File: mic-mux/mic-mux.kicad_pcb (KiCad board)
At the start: 4 copper layers, 312 parts, among them J23 Extra GPIO, U124 OPA1604, U125 DS1882, U126 OPA1604, U127 DS1882, U128 OPA1604, U129 DS1882, U130 OPA1604, U131 DS1882, U146 OPA1604, U147 OPA1602, U148 OPA1604, U149 OPA1604, U150 OPA1604, U151 OPA1604, U152 OPA1602, U153 OPA1604, U154 OPA1604, U155 OPA1604, U156 OPA1604, U157 OPA1602, U158 OPA1604, U159 OPA1604, U160 OPA1604, U161 OPA1604, U162 OPA1602, U163 OPA1604, U164 OPA1604, U165 OPA1604, U18 ADG708, U2 ADG715, U20 ADG708, U22 ADG708, U24 ADG708, U27 ADG708, U29 ADG708, U33 ADG708, U35 TCA9555, U37 ADG708, U38 TCA9555

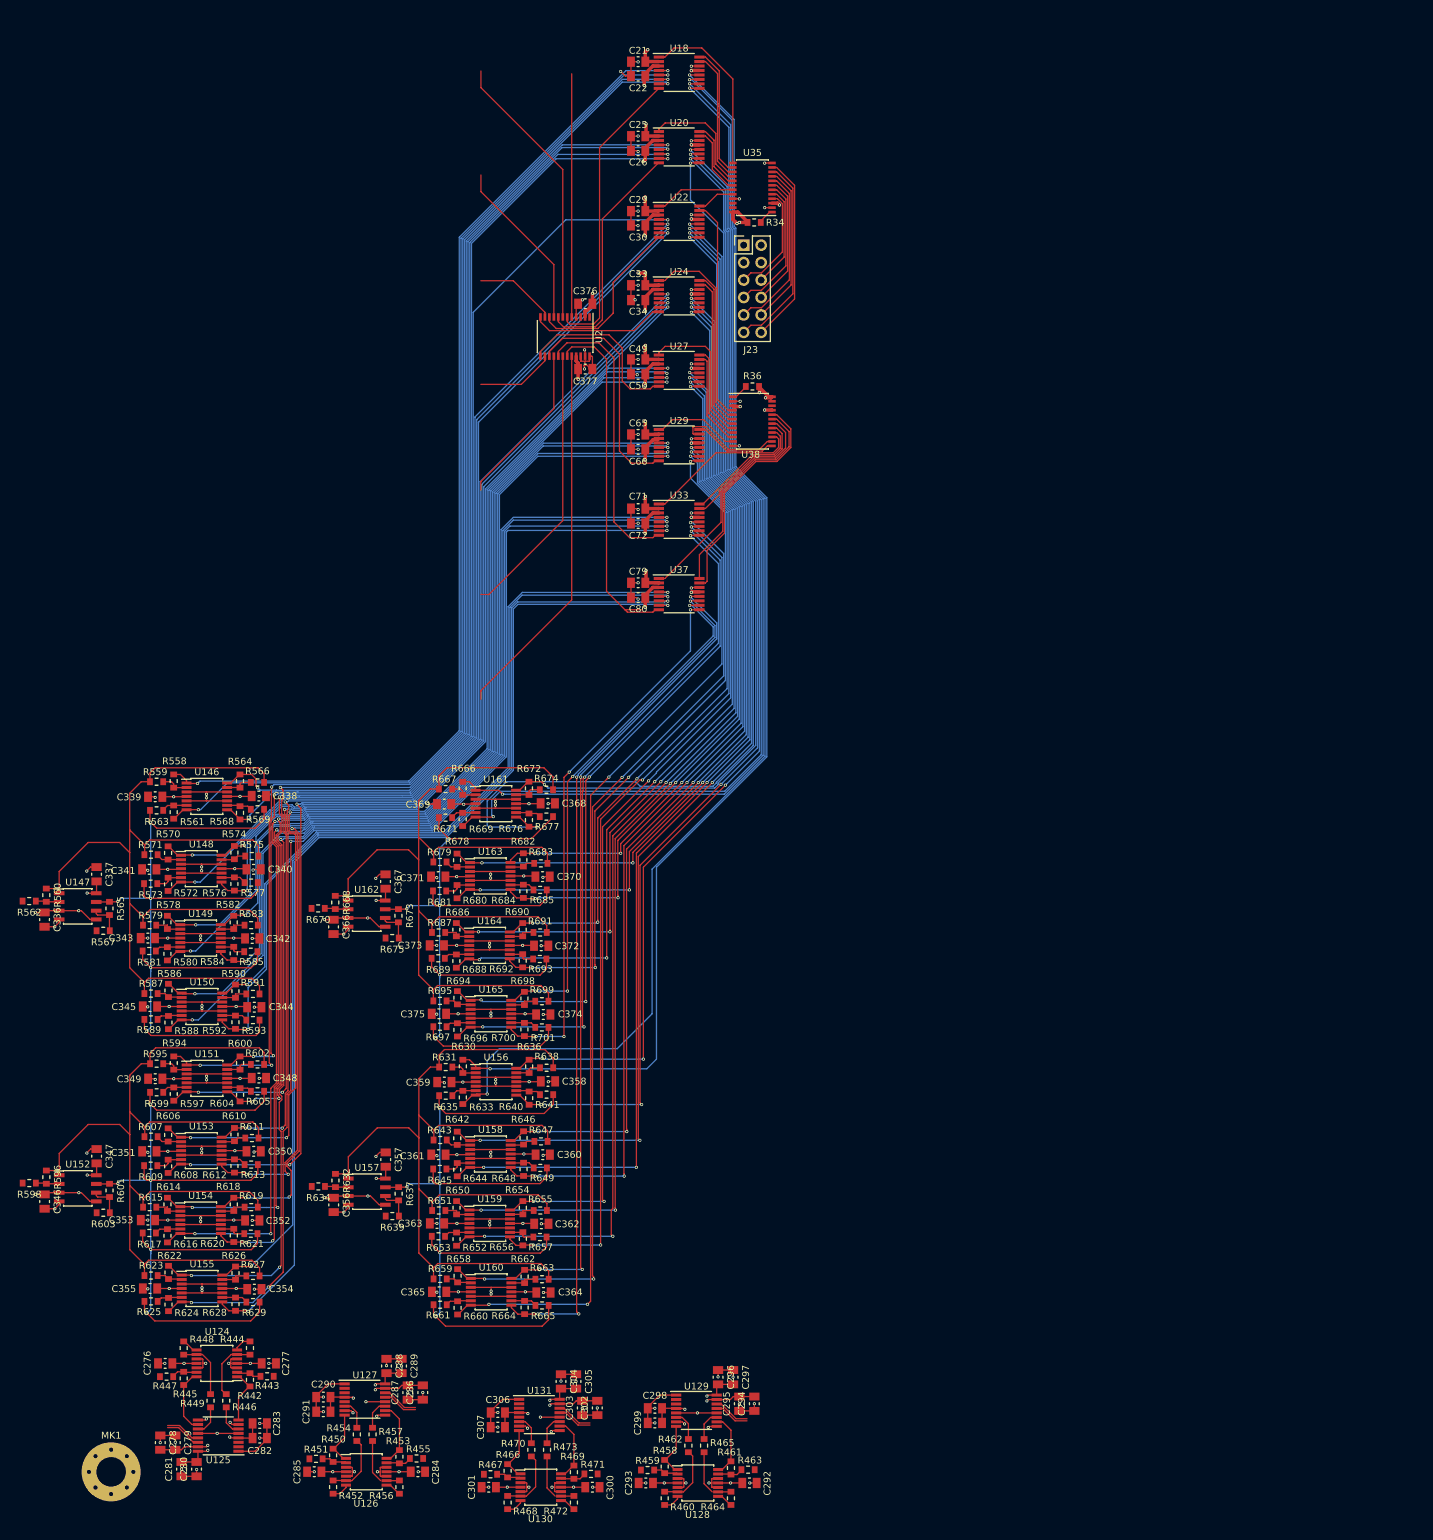
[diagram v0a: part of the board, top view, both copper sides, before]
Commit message: Re annotating entire schematic. This time properly
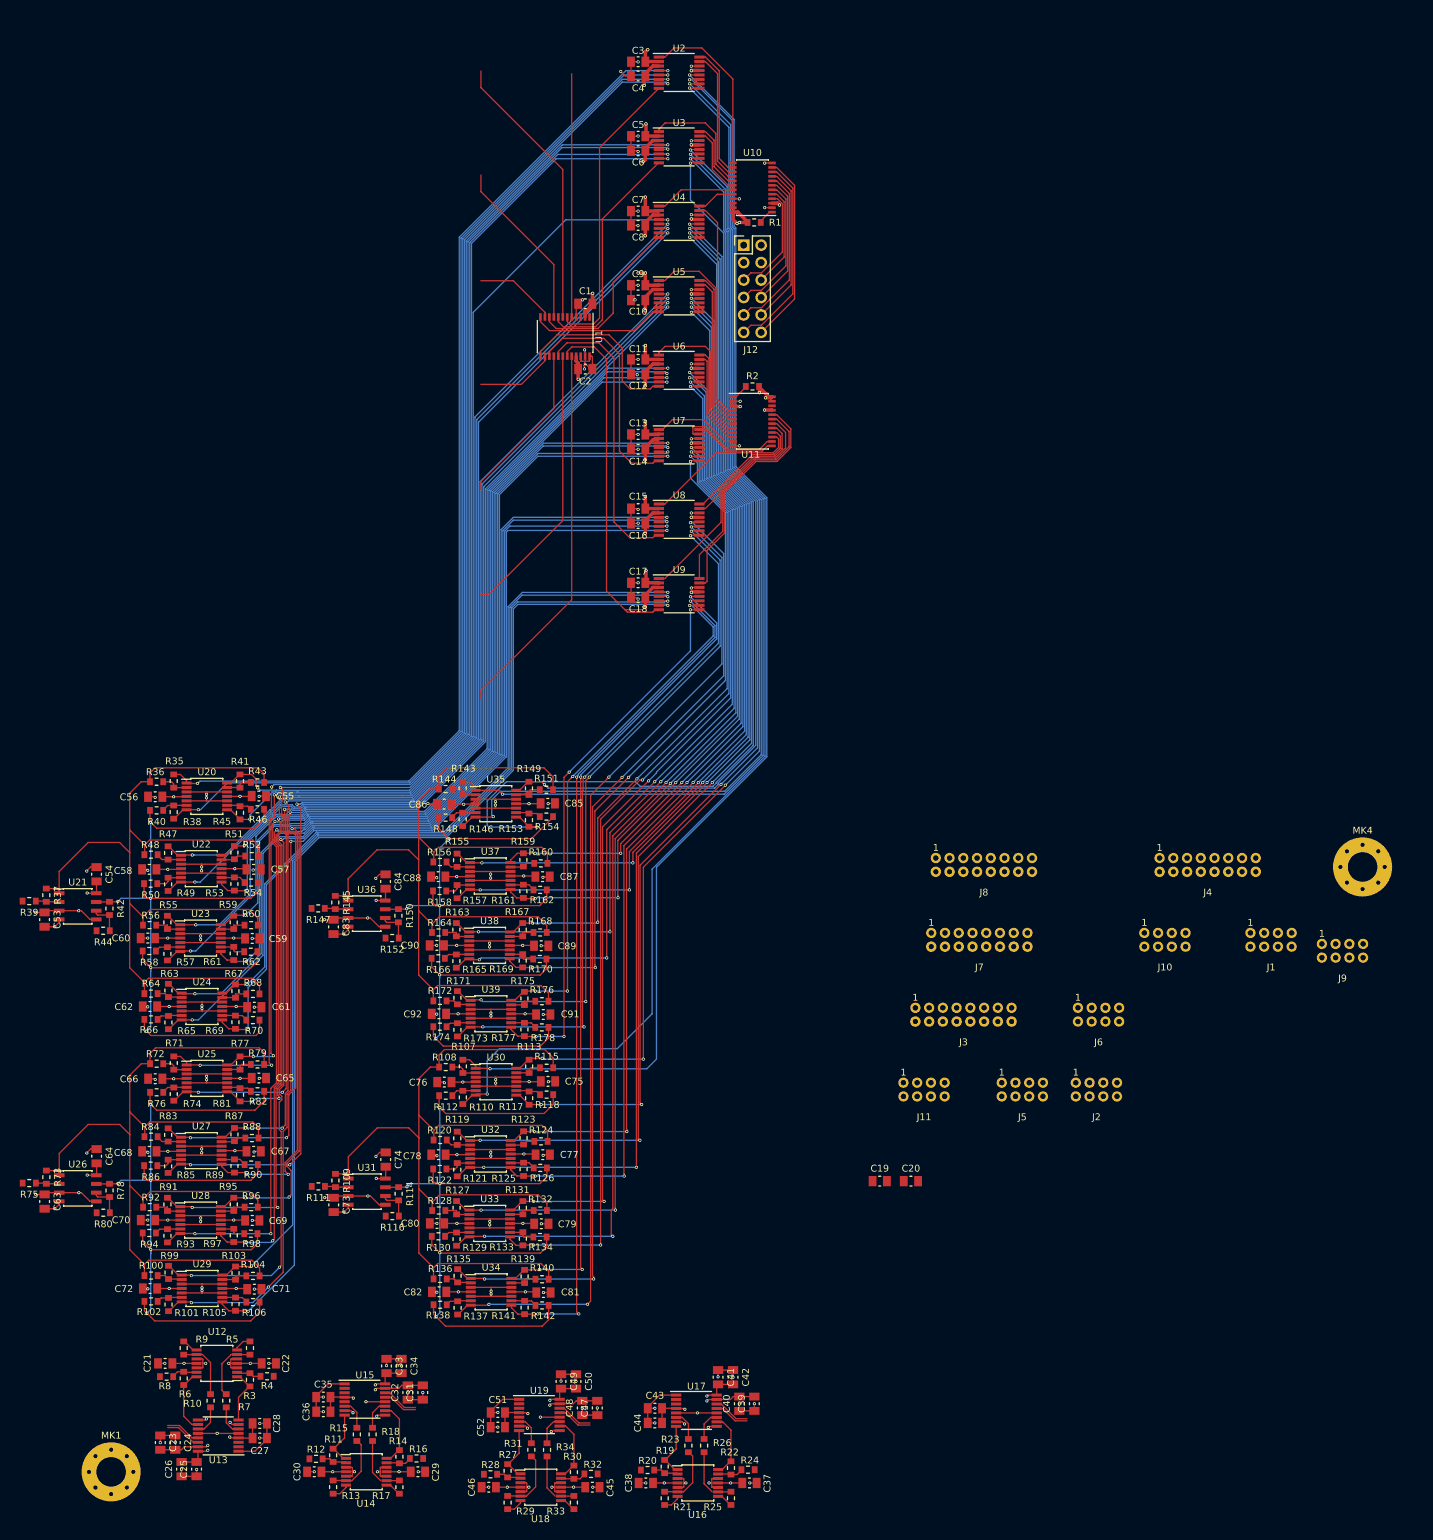
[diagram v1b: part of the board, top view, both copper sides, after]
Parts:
- added C19: 0.1uF, Capacitor_SMD:C_0805_2012Metric_Pad1.15x1.50mm_HandSolder, F.Cu at (307.5, 325.6)
- added C20: 0.1uF, Capacitor_SMD:C_0805_2012Metric_Pad1.15x1.50mm_HandSolder, F.Cu at (312.0, 325.6)
- added J1: MIC-IN, SW-Hirose:DF11-8DS-2DSA, F.Cu at (364.4, 290.5)
- added J10: I2C and Reset (Top-Male), SW-Hirose:DF11-8DP-2DSA, F.Cu at (349.0, 290.5)
- added J11: Power Out (Top-Male), SW-Hirose:DF11-8DP-2DSA, F.Cu at (313.9, 312.3)
- added J2: MIC-OUT, SW-Hirose:DF11-8DS-2DSA, F.Cu at (339.0, 312.3)
- added J3: Headphone MUX Audio IN (Top-Male), SW-Hirose:DF11-16DP-2DSA, F.Cu at (319.6, 301.4)
- added J4: Headphone MUX Audio OUT (Top-Male), SW-Hirose:DF11-16DP-2DSA, F.Cu at (355.2, 279.6)
- added J5: I2C and Reset, SW-Hirose:DF11-8DS-2DSA, F.Cu at (328.2, 312.3)
- added J6: Power In, SW-Hirose:DF11-8DS-2DSA, F.Cu at (339.3, 301.4)
- added J7: Headphone MUX Audio IN (Bottom-Female), SW-Hirose:DF11-16DS-2DSA, F.Cu at (322.0, 290.5)
- added J8: Headphone MUX Audio OUT (Bottom-Female), SW-Hirose:DF11-16DS-2DSA, F.Cu at (322.6, 279.6)
- added J9: GND, SW-Hirose:DF11-8DS-2DSA, F.Cu at (374.8, 292.1)
- added MK4: Mounting_Hole_PAD, MountingHole:MountingHole_4.3mm_M4_Pad_Via, F.Cu at (377.7, 279.9)
- renumbered C376 to C1, C34 to C10, C49 to C11, C50 to C12, C65 to C13, C66 to C14, C71 to C15, C72 to C16, C79 to C17, C80 to C18, C377 to C2, C276 to C21, C277 to C22, C278 to C23, C279 to C24, C280 to C25, C281 to C26, C282 to C27, C283 to C28, C284 to C29, C21 to C3, C285 to C30, C286 to C31, C287 to C32, C288 to C33, C289 to C34, C290 to C35, C291 to C36, C292 to C37, C293 to C38, C294 to C39, C22 to C4, C295 to C40, C296 to C41, C297 to C42, C298 to C43, C299 to C44, C300 to C45, C301 to C46, C302 to C47, C303 to C48, C304 to C49, C25 to C5, C305 to C50, C306 to C51, C307 to C52, C336 to C53, C337 to C54, C338 to C55, C339 to C56, C340 to C57, C341 to C58, C342 to C59, C26 to C6, C343 to C60, C344 to C61, C345 to C62, C346 to C63, C347 to C64, C348 to C65, C349 to C66, C350 to C67, C351 to C68, C352 to C69, C29 to C7, C353 to C70, C354 to C71, C355 to C72, C356 to C73, C357 to C74, C358 to C75, C359 to C76, C360 to C77, C361 to C78, C362 to C79, C30 to C8, C363 to C80, C364 to C81, C365 to C82, C366 to C83, C367 to C84, C368 to C85, C369 to C86, C370 to C87, C371 to C88, C372 to C89, C33 to C9, C373 to C90, C374 to C91, C375 to C92, J23 to J12, R34 to R1, R449 to R10, R623 to R100, R624 to R101, R625 to R102, R626 to R103, R627 to R104, R628 to R105, R629 to R106, R630 to R107, R631 to R108, R632 to R109, R450 to R11, R633 to R110, R634 to R111, R635 to R112, R636 to R113, R637 to R114, R638 to R115, R639 to R116, R640 to R117, R641 to R118, R642 to R119, R451 to R12, R643 to R120, R644 to R121, R645 to R122, R646 to R123, R647 to R124, R648 to R125, R649 to R126, R650 to R127, R651 to R128, R652 to R129, R452 to R13, R653 to R130, R654 to R131, R655 to R132, R656 to R133, R657 to R134, R658 to R135, R659 to R136, R660 to R137, R661 to R138, R662 to R139, R453 to R14, R663 to R140, R664 to R141, R665 to R142, R666 to R143, R667 to R144, R668 to R145, R669 to R146, R670 to R147, R671 to R148, R672 to R149, R454 to R15, R673 to R150, R674 to R151, R675 to R152, R676 to R153, R677 to R154, R678 to R155, R679 to R156, R680 to R157, R681 to R158, R682 to R159, R455 to R16, R683 to R160, R684 to R161, R685 to R162, R686 to R163, R687 to R164, R688 to R165, R689 to R166, R690 to R167, R691 to R168, R692 to R169, R456 to R17, R693 to R170, R694 to R171, R695 to R172, R696 to R173, R697 to R174, R698 to R175, R699 to R176, R700 to R177, R701 to R178, R457 to R18, R458 to R19, R36 to R2, R459 to R20, R460 to R21, R461 to R22, R462 to R23, R463 to R24, R464 to R25, R465 to R26, R466 to R27, R467 to R28, R468 to R29, R442 to R3, R469 to R30, R470 to R31, R471 to R32, R472 to R33, R473 to R34, R558 to R35, R559 to R36, R560 to R37, R561 to R38, R562 to R39, R443 to R4, R563 to R40, R564 to R41, R565 to R42, R566 to R43, R567 to R44, R568 to R45, R569 to R46, R570 to R47, R571 to R48, R572 to R49, R444 to R5, R573 to R50, R574 to R51, R575 to R52, R576 to R53, R577 to R54, R578 to R55, R579 to R56, R580 to R57, R581 to R58, R582 to R59, R445 to R6, R583 to R60, R584 to R61, R585 to R62, R586 to R63, R587 to R64, R588 to R65, R589 to R66, R590 to R67, R591 to R68, R592 to R69, R446 to R7, R593 to R70, R594 to R71, R595 to R72, R596 to R73, R597 to R74, R598 to R75, R599 to R76, R600 to R77, R601 to R78, R602 to R79, R447 to R8, R603 to R80, R604 to R81, R605 to R82, R606 to R83, R607 to R84, R608 to R85, R609 to R86, R610 to R87, R611 to R88, R612 to R89, R448 to R9, R613 to R90, R614 to R91, R615 to R92, R616 to R93, R617 to R94, R618 to R95, R619 to R96, R620 to R97, R621 to R98, R622 to R99, U2 to U1, U35 to U10, U38 to U11, U124 to U12, U125 to U13, U126 to U14, U127 to U15, U128 to U16, U129 to U17, U130 to U18, U131 to U19, U18 to U2, U146 to U20, U147 to U21, U148 to U22, U149 to U23, U150 to U24, U151 to U25, U152 to U26, U153 to U27, U154 to U28, U155 to U29, U20 to U3, U156 to U30, U157 to U31, U158 to U32, U159 to U33, U160 to U34, U161 to U35, U162 to U36, U163 to U37, U164 to U38, U165 to U39, U22 to U4, U24 to U5, U27 to U6, U29 to U7, U33 to U8, U37 to U9
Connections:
- net +12V renamed +12VA
- net /Audio Mux and Control/2v5-SCL-0 renamed /2v5-SCL-0
- net /Audio Mux and Control/2v5-SDA-0 renamed /2v5-SDA-0
- net /Audio Mux and Control/5V-SCL-1 renamed /5V-SCL-1
- net /Audio Mux and Control/5V-SDA-1 renamed /5V-SDA-1
- net /Audio Mux and Control/AMP-MIC-IN-0-0 renamed /Mic Mux and Control/AMP-MIC-IN-0-0
- net /Audio Mux and Control/AMP-MIC-IN-0-1 renamed /Mic Mux and Control/AMP-MIC-IN-0-1
- net /Audio Mux and Control/AMP-MIC-IN-0-2 renamed /Mic Mux and Control/AMP-MIC-IN-0-2
- net /Audio Mux and Control/AMP-MIC-IN-0-3 renamed /Mic Mux and Control/AMP-MIC-IN-0-3
- net /Audio Mux and Control/AMP-MIC-IN-0-4 renamed /Mic Mux and Control/AMP-MIC-IN-0-4
- net /Audio Mux and Control/AMP-MIC-IN-0-5 renamed /Mic Mux and Control/AMP-MIC-IN-0-5
- net /Audio Mux and Control/AMP-MIC-IN-0-6 renamed /Mic Mux and Control/AMP-MIC-IN-0-6
- net /Audio Mux and Control/AMP-MIC-IN-0-7 renamed /Mic Mux and Control/AMP-MIC-IN-0-7
- net /Audio Mux and Control/AMP-MIC-IN-1-0 renamed /Mic Mux and Control/AMP-MIC-IN-1-0
- net /Audio Mux and Control/AMP-MIC-IN-1-1 renamed /Mic Mux and Control/AMP-MIC-IN-1-1
- net /Audio Mux and Control/AMP-MIC-IN-1-2 renamed /Mic Mux and Control/AMP-MIC-IN-1-2
- net /Audio Mux and Control/AMP-MIC-IN-1-3 renamed /Mic Mux and Control/AMP-MIC-IN-1-3
- net /Audio Mux and Control/AMP-MIC-IN-1-4 renamed /Mic Mux and Control/AMP-MIC-IN-1-4
- net /Audio Mux and Control/AMP-MIC-IN-1-5 renamed /Mic Mux and Control/AMP-MIC-IN-1-5
- net /Audio Mux and Control/AMP-MIC-IN-1-6 renamed /Mic Mux and Control/AMP-MIC-IN-1-6
- net /Audio Mux and Control/AMP-MIC-IN-1-7 renamed /Mic Mux and Control/AMP-MIC-IN-1-7
- net /Audio Mux and Control/AMP-MIC-IN-2-0 renamed /Mic Mux and Control/AMP-MIC-IN-2-0
- net /Audio Mux and Control/AMP-MIC-IN-2-1 renamed /Mic Mux and Control/AMP-MIC-IN-2-1
- net /Audio Mux and Control/AMP-MIC-IN-2-2 renamed /Mic Mux and Control/AMP-MIC-IN-2-2
- net /Audio Mux and Control/AMP-MIC-IN-2-3 renamed /Mic Mux and Control/AMP-MIC-IN-2-3
- net /Audio Mux and Control/AMP-MIC-IN-2-4 renamed /Mic Mux and Control/AMP-MIC-IN-2-4
- net /Audio Mux and Control/AMP-MIC-IN-2-5 renamed /Mic Mux and Control/AMP-MIC-IN-2-5
- net /Audio Mux and Control/AMP-MIC-IN-2-6 renamed /Mic Mux and Control/AMP-MIC-IN-2-6
- net /Audio Mux and Control/AMP-MIC-IN-2-7 renamed /Mic Mux and Control/AMP-MIC-IN-2-7
- net /Audio Mux and Control/AMP-MIC-IN-3-0 renamed /Mic Mux and Control/AMP-MIC-IN-3-0
- net /Audio Mux and Control/AMP-MIC-IN-3-1 renamed /Mic Mux and Control/AMP-MIC-IN-3-1
- net /Audio Mux and Control/AMP-MIC-IN-3-2 renamed /Mic Mux and Control/AMP-MIC-IN-3-2
- net /Audio Mux and Control/AMP-MIC-IN-3-3 renamed /Mic Mux and Control/AMP-MIC-IN-3-3
- net /Audio Mux and Control/AMP-MIC-IN-3-4 renamed /Mic Mux and Control/AMP-MIC-IN-3-4
- net /Audio Mux and Control/AMP-MIC-IN-3-5 renamed /Mic Mux and Control/AMP-MIC-IN-3-5
- net /Audio Mux and Control/AMP-MIC-IN-3-6 renamed /Mic Mux and Control/AMP-MIC-IN-3-6
- net /Audio Mux and Control/AMP-MIC-IN-3-7 renamed /Mic Mux and Control/AMP-MIC-IN-3-7
- net /Audio Mux and Control/AMP-MIC-IN-4-0 renamed /Mic Mux and Control/AMP-MIC-IN-4-0
- net /Audio Mux and Control/AMP-MIC-IN-4-1 renamed /Mic Mux and Control/AMP-MIC-IN-4-1
- net /Audio Mux and Control/AMP-MIC-IN-4-2 renamed /Mic Mux and Control/AMP-MIC-IN-4-2
- net /Audio Mux and Control/AMP-MIC-IN-4-3 renamed /Mic Mux and Control/AMP-MIC-IN-4-3
- net /Audio Mux and Control/AMP-MIC-IN-4-4 renamed /Mic Mux and Control/AMP-MIC-IN-4-4
- net /Audio Mux and Control/AMP-MIC-IN-4-5 renamed /Mic Mux and Control/AMP-MIC-IN-4-5
- net /Audio Mux and Control/AMP-MIC-IN-4-6 renamed /Mic Mux and Control/AMP-MIC-IN-4-6
- net /Audio Mux and Control/AMP-MIC-IN-4-7 renamed /Mic Mux and Control/AMP-MIC-IN-4-7
- net /Audio Mux and Control/AMP-MIC-IN-5-0 renamed /Mic Mux and Control/AMP-MIC-IN-5-0
- net /Audio Mux and Control/AMP-MIC-IN-5-1 renamed /Mic Mux and Control/AMP-MIC-IN-5-1
- net /Audio Mux and Control/AMP-MIC-IN-5-2 renamed /Mic Mux and Control/AMP-MIC-IN-5-2
- net /Audio Mux and Control/AMP-MIC-IN-5-3 renamed /Mic Mux and Control/AMP-MIC-IN-5-3
- net /Audio Mux and Control/AMP-MIC-IN-5-4 renamed /Mic Mux and Control/AMP-MIC-IN-5-4
- net /Audio Mux and Control/AMP-MIC-IN-5-5 renamed /Mic Mux and Control/AMP-MIC-IN-5-5
- net /Audio Mux and Control/AMP-MIC-IN-5-6 renamed /Mic Mux and Control/AMP-MIC-IN-5-6
- net /Audio Mux and Control/AMP-MIC-IN-5-7 renamed /Mic Mux and Control/AMP-MIC-IN-5-7
- net /Audio Mux and Control/AMP-MIC-IN-6-0 renamed /Mic Mux and Control/AMP-MIC-IN-6-0
- net /Audio Mux and Control/AMP-MIC-IN-6-1 renamed /Mic Mux and Control/AMP-MIC-IN-6-1
- net /Audio Mux and Control/AMP-MIC-IN-6-2 renamed /Mic Mux and Control/AMP-MIC-IN-6-2
- net /Audio Mux and Control/AMP-MIC-IN-6-3 renamed /Mic Mux and Control/AMP-MIC-IN-6-3
- net /Audio Mux and Control/AMP-MIC-IN-6-4 renamed /Mic Mux and Control/AMP-MIC-IN-6-4
- net /Audio Mux and Control/AMP-MIC-IN-6-5 renamed /Mic Mux and Control/AMP-MIC-IN-6-5
- net /Audio Mux and Control/AMP-MIC-IN-6-6 renamed /Mic Mux and Control/AMP-MIC-IN-6-6
- net /Audio Mux and Control/AMP-MIC-IN-6-7 renamed /Mic Mux and Control/AMP-MIC-IN-6-7
- net /Audio Mux and Control/AMP-MIC-IN-7-0 renamed /Mic Mux and Control/AMP-MIC-IN-7-0
- net /Audio Mux and Control/AMP-MIC-IN-7-1 renamed /Mic Mux and Control/AMP-MIC-IN-7-1
- net /Audio Mux and Control/AMP-MIC-IN-7-2 renamed /Mic Mux and Control/AMP-MIC-IN-7-2
- net /Audio Mux and Control/AMP-MIC-IN-7-3 renamed /Mic Mux and Control/AMP-MIC-IN-7-3
- net /Audio Mux and Control/AMP-MIC-IN-7-4 renamed /Mic Mux and Control/AMP-MIC-IN-7-4
- net /Audio Mux and Control/AMP-MIC-IN-7-5 renamed /Mic Mux and Control/AMP-MIC-IN-7-5
- net /Audio Mux and Control/AMP-MIC-IN-7-6 renamed /Mic Mux and Control/AMP-MIC-IN-7-6
- net /Audio Mux and Control/AMP-MIC-IN-7-7 renamed /Mic Mux and Control/AMP-MIC-IN-7-7
- net /Audio Mux and Control/DEV-MIC-IN-XBAR-CTL0 renamed /Mic Mux and Control/DEV-MIC-IN-XBAR-CTL0
- net /Audio Mux and Control/DEV-MIC-IN-XBAR-CTL1 renamed /Mic Mux and Control/DEV-MIC-IN-XBAR-CTL1
- net /Audio Mux and Control/DEV-MIC-IN-XBAR-CTL10 renamed /Mic Mux and Control/DEV-MIC-IN-XBAR-CTL10
- net /Audio Mux and Control/DEV-MIC-IN-XBAR-CTL11 renamed /Mic Mux and Control/DEV-MIC-IN-XBAR-CTL11
- net /Audio Mux and Control/DEV-MIC-IN-XBAR-CTL12 renamed /Mic Mux and Control/DEV-MIC-IN-XBAR-CTL12
- net /Audio Mux and Control/DEV-MIC-IN-XBAR-CTL13 renamed /Mic Mux and Control/DEV-MIC-IN-XBAR-CTL13
- net /Audio Mux and Control/DEV-MIC-IN-XBAR-CTL14 renamed /Mic Mux and Control/DEV-MIC-IN-XBAR-CTL14
- net /Audio Mux and Control/DEV-MIC-IN-XBAR-CTL15 renamed /Mic Mux and Control/DEV-MIC-IN-XBAR-CTL15
- net /Audio Mux and Control/DEV-MIC-IN-XBAR-CTL16 renamed /Mic Mux and Control/DEV-MIC-IN-XBAR-CTL16
- net /Audio Mux and Control/DEV-MIC-IN-XBAR-CTL17 renamed /Mic Mux and Control/DEV-MIC-IN-XBAR-CTL17
- net /Audio Mux and Control/DEV-MIC-IN-XBAR-CTL18 renamed /Mic Mux and Control/DEV-MIC-IN-XBAR-CTL18
- net /Audio Mux and Control/DEV-MIC-IN-XBAR-CTL19 renamed /Mic Mux and Control/DEV-MIC-IN-XBAR-CTL19
- net /Audio Mux and Control/DEV-MIC-IN-XBAR-CTL2 renamed /Mic Mux and Control/DEV-MIC-IN-XBAR-CTL2
- net /Audio Mux and Control/DEV-MIC-IN-XBAR-CTL20 renamed /Mic Mux and Control/DEV-MIC-IN-XBAR-CTL20
- net /Audio Mux and Control/DEV-MIC-IN-XBAR-CTL21 renamed /Mic Mux and Control/DEV-MIC-IN-XBAR-CTL21
- net /Audio Mux and Control/DEV-MIC-IN-XBAR-CTL22 renamed /Mic Mux and Control/DEV-MIC-IN-XBAR-CTL22
- net /Audio Mux and Control/DEV-MIC-IN-XBAR-CTL23 renamed /Mic Mux and Control/DEV-MIC-IN-XBAR-CTL23
- net /Audio Mux and Control/DEV-MIC-IN-XBAR-CTL3 renamed /Mic Mux and Control/DEV-MIC-IN-XBAR-CTL3
- net /Audio Mux and Control/DEV-MIC-IN-XBAR-CTL4 renamed /Mic Mux and Control/DEV-MIC-IN-XBAR-CTL4
- net /Audio Mux and Control/DEV-MIC-IN-XBAR-CTL5 renamed /Mic Mux and Control/DEV-MIC-IN-XBAR-CTL5
- net /Audio Mux and Control/DEV-MIC-IN-XBAR-CTL6 renamed /Mic Mux and Control/DEV-MIC-IN-XBAR-CTL6
- net /Audio Mux and Control/DEV-MIC-IN-XBAR-CTL7 renamed /Mic Mux and Control/DEV-MIC-IN-XBAR-CTL7
- net /Audio Mux and Control/DEV-MIC-IN-XBAR-CTL8 renamed /Mic Mux and Control/DEV-MIC-IN-XBAR-CTL8
- net /Audio Mux and Control/DEV-MIC-IN-XBAR-CTL9 renamed /Mic Mux and Control/DEV-MIC-IN-XBAR-CTL9
- net /Audio Mux and Control/Dual Mic Distro Amp 0/L_Distro_Bus renamed /Mic Mux and Control/Dual Mic Distro Amp 0/L_Distro_Bus
- net /Audio Mux and Control/Dual Mic Distro Amp 0/L_IN renamed /Mic Mux and Control/Dual Mic Distro Amp 0/L_IN
- net /Audio Mux and Control/Dual Mic Distro Amp 0/R_Distro_Bus renamed /Mic Mux and Control/Dual Mic Distro Amp 0/R_Distro_Bus
- net /Audio Mux and Control/Dual Mic Distro Amp 0/R_IN renamed /Mic Mux and Control/Dual Mic Distro Amp 0/R_IN
- net /Audio Mux and Control/Dual Mic Distro Amp 1/L_Distro_Bus renamed /Mic Mux and Control/Dual Mic Distro Amp 1/L_Distro_Bus
- net /Audio Mux and Control/Dual Mic Distro Amp 1/L_IN renamed /Mic Mux and Control/Dual Mic Distro Amp 1/L_IN
- net /Audio Mux and Control/Dual Mic Distro Amp 1/R_Distro_Bus renamed /Mic Mux and Control/Dual Mic Distro Amp 1/R_Distro_Bus
- net /Audio Mux and Control/Dual Mic Distro Amp 1/R_IN renamed /Mic Mux and Control/Dual Mic Distro Amp 1/R_IN
- net /Audio Mux and Control/Dual Mic Distro Amp 2/L_Distro_Bus renamed /Mic Mux and Control/Dual Mic Distro Amp 2/L_Distro_Bus
- net /Audio Mux and Control/Dual Mic Distro Amp 2/L_IN renamed /Mic Mux and Control/Dual Mic Distro Amp 2/L_IN
- net /Audio Mux and Control/Dual Mic Distro Amp 2/R_Distro_Bus renamed /Mic Mux and Control/Dual Mic Distro Amp 2/R_Distro_Bus
- net /Audio Mux and Control/Dual Mic Distro Amp 2/R_IN renamed /Mic Mux and Control/Dual Mic Distro Amp 2/R_IN
- net /Audio Mux and Control/Dual Mic Distro Amp 3/L_Distro_Bus renamed /Mic Mux and Control/Dual Mic Distro Amp 3/L_Distro_Bus
- net /Audio Mux and Control/Dual Mic Distro Amp 3/L_IN renamed /Mic Mux and Control/Dual Mic Distro Amp 3/L_IN
- net /Audio Mux and Control/Dual Mic Distro Amp 3/R_Distro_Bus renamed /Mic Mux and Control/Dual Mic Distro Amp 3/R_Distro_Bus
- net /Audio Mux and Control/Dual Mic Distro Amp 3/R_IN renamed /Mic Mux and Control/Dual Mic Distro Amp 3/R_IN
- R12 pad 2: /Audio Mux and Control/MIC-IN-2 -> /MIC-IN2
- R16 pad 2: /Audio Mux and Control/MIC-IN-3 -> /MIC-IN3
- R20 pad 2: /Audio Mux and Control/MIC-IN-4 -> /MIC-IN4
- R24 pad 2: /Audio Mux and Control/MIC-IN-5 -> /MIC-IN5
- R28 pad 2: /Audio Mux and Control/MIC-IN-6 -> /MIC-IN6
- R32 pad 2: /Audio Mux and Control/MIC-IN-7 -> /MIC-IN7
- R4 pad 2: /Audio Mux and Control/MIC-IN-0 -> /MIC-IN0
- R8 pad 2: /Audio Mux and Control/MIC-IN-1 -> /MIC-IN1
- U1 pad 11: Net-(C32-Pad1) -> /MIC-OUT3
- U1 pad 14: Net-(C42-Pad1) -> /MIC-OUT4
- U1 pad 16: Net-(C58-Pad1) -> /MIC-OUT5
- U1 pad 18: Net-(C69-Pad1) -> /MIC-OUT6
- U1 pad 20: Net-(C76-Pad1) -> /MIC-OUT7
- U1 pad 23: /Arduino Nano Header Connections + Ethernet connection/D2_SPST -> /SPST-~RST
- U1 pad 5: Net-(C20-Pad1) -> /MIC-OUT0
- U1 pad 7: Net-(C24-Pad1) -> /MIC-OUT1
- U1 pad 9: Net-(C28-Pad1) -> /MIC-OUT2
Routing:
- net Net-(C76-Pad1): track 55.4 -> 0.00 mm
- net /MIC-OUT7: track 0.00 -> 55.4 mm
- net Net-(C24-Pad1): track 40.7 -> 0.00 mm
- net /MIC-OUT1: track 0.00 -> 40.7 mm
- net Net-(C69-Pad1): track 40.3 -> 0.00 mm
- net /MIC-OUT6: track 0.00 -> 40.3 mm
- net Net-(C20-Pad1): track 35.4 -> 0.00 mm
- net /MIC-OUT0: track 0.00 -> 35.4 mm
- net Net-(C28-Pad1): track 25.1 -> 0.00 mm
- net /MIC-OUT2: track 0.00 -> 25.1 mm
- net Net-(C58-Pad1): track 23.9 -> 0.00 mm
- net /MIC-OUT5: track 0.00 -> 23.9 mm
- net Net-(C32-Pad1): track 11.9 -> 0.00 mm
- net /MIC-OUT3: track 0.00 -> 11.9 mm
- net Net-(C42-Pad1): track 11.4 -> 0.00 mm
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- added copper zone on In1.Cu, net +12V
- removed copper zone on In1.Cu, net +12VA

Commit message: initial mic mux pcb layout stuff and changing text size in schematic
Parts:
- removed MK5: Mounting_Hole_PAD, MountingHole:MountingHole_4.3mm_M4_Pad_Via
- moved MK3 388.4 mm to (50.8, 127.0)
- moved J2 296.4 mm to (71.8, 184.0)
- moved MK2 265.3 mm to (177.8, 355.6)
- moved MK4 251.7 mm to (177.8, 127.0)
- moved C10 161.8 mm to (114.0, 163.8)
- moved C11 161.8 mm to (114.0, 172.5)
- moved C12 161.8 mm to (114.0, 174.6)
- moved C13 161.8 mm to (114.0, 183.4)
- moved C14 161.8 mm to (114.0, 185.5)
- moved C15 161.8 mm to (114.0, 194.2)
- moved C16 161.8 mm to (114.0, 196.3)
- moved C17 161.8 mm to (114.0, 205.0)
- moved C18 161.8 mm to (114.0, 207.1)
- moved C19 161.8 mm to (149.2, 292.1)
- moved C20 161.8 mm to (153.8, 292.1)
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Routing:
- removed copper zone on In2.Cu, net GNDREF

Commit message: positioning connectors and mounting holes
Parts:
- J12: footprint Connector_PinHeader_2.54mm:PinHeader_2x06_P2.54mm_Vertical -> SW-Hirose:DF11-12DP-2DS
- J8: moved to B.Cu
- moved J4 151.4 mm to (127.0, 111.8)
- moved J8 134.5 mm to (127.0, 116.8)
- moved J9 124.7 mm to (134.7, 352.5)
- moved J1 124.7 mm to (124.3, 350.9)
- moved J10 124.7 mm to (108.8, 350.9)
- moved J5 104.6 mm to (103.3, 359.4)
- moved C19 100.0 mm to (135.2, 193.0)
- moved C20 100.0 mm to (139.8, 193.0)
- moved J3 80.6 mm to (160.8, 348.5)
- moved J6 80.6 mm to (180.4, 348.5)
- moved J7 80.6 mm to (163.1, 337.6)
- moved J2 75.0 mm to (127.0, 133.3), turned to 180 degrees
- moved J12 71.9 mm to (190.5, 193.7), turned to 90 degrees
- moved C3 70.5 mm to (172.9, 168.0), turned to 90 degrees
- moved J11 68.2 mm to (88.9, 292.7)
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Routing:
- net /Mic Mux and Control/AMP-MIC-IN-0-0: track 159.0 -> 4.71 mm, vias 2 -> 1
- net /Mic Mux and Control/AMP-MIC-IN-1-0: track 160.1 -> 9.99 mm, vias 2 -> 1
- net /Mic Mux and Control/AMP-MIC-IN-2-0: track 199.5 -> 56.3 mm, vias 4 -> 3
- net /Mic Mux and Control/AMP-MIC-IN-3-0: track 203.8 -> 61.8 mm, vias 4 -> 3
- net /Mic Mux and Control/AMP-MIC-IN-0-1: track 148.5 -> 9.29 mm, vias 2 -> 1
- net /Mic Mux and Control/AMP-MIC-IN-2-1: track 184.9 -> 47.8 mm, vias 4 -> 3
- net /Mic Mux and Control/AMP-MIC-IN-1-1: track 149.2 -> 13.1 mm, vias 2 -> 1
- net /Mic Mux and Control/AMP-MIC-IN-3-1: track 191.7 -> 56.4 mm, vias 4 -> 3
- net /Mic Mux and Control/AMP-MIC-IN-4-0: track 185.5 -> 57.5 mm, vias 2 -> 1
- net /Mic Mux and Control/AMP-MIC-IN-5-0: track 184.8 -> 56.9 mm, vias 2 -> 1
- net /Mic Mux and Control/AMP-MIC-IN-0-2: track 149.1 -> 21.4 mm, vias 2 -> 1
- net /Mic Mux and Control/AMP-MIC-IN-1-2: track 141.6 -> 22.8 mm, vias 2 -> 1
- net /Mic Mux and Control/AMP-MIC-IN-2-2: track 187.1 -> 68.9 mm, vias 4 -> 3
- net /Mic Mux and Control/AMP-MIC-IN-3-2: track 188.4 -> 72.5 mm, vias 4 -> 3
- net /Mic Mux and Control/AMP-MIC-IN-6-0: track 150.7 -> 39.0 mm, vias 2 -> 1
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- added copper zone on In2.Cu, net GNDREF
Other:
- board outline added: 142.2 x 218.4 mm

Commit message: Finished re alignment of left side of distro amps
Starting re alignment of right side of distro amps

My kingdom for asethetics
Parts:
- J2, J5, J6, J7: moved to B.Cu
- moved C27 121.9 mm to (220.9, 316.1)
- moved C28 121.9 mm to (220.9, 314.0)
- moved C32 121.9 mm to (242.4, 309.5)
- moved C34 121.9 mm to (241.5, 305.6)
- moved C35 121.9 mm to (230.1, 310.2)
- moved C36 121.9 mm to (230.1, 312.3)
- moved C39 121.9 mm to (292.9, 311.1)
- moved C43 121.9 mm to (278.4, 311.8)
- moved C44 121.9 mm to (278.4, 313.9)
- moved C48 121.9 mm to (267.8, 311.8)
- moved C50 121.9 mm to (266.9, 307.9)
- moved R10 121.9 mm to (213.7, 310.7)
- moved R12 121.9 mm to (229.1, 319.2)
- moved R14 121.9 mm to (241.2, 318.9)
- moved R17 121.9 mm to (241.2, 323.3)
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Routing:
- net GNDREF: track 481.2 -> 215.9 mm, vias 159 -> 139
- net /Mic Mux and Control/Dual Mic Distro Amp 3/L_Distro_Bus: track 137.9 -> 0.00 mm
- net /Mic Mux and Control/Dual Mic Distro Amp 2/L_Distro_Bus: track 137.1 -> 0.00 mm
- net /Mic Mux and Control/Dual Mic Distro Amp 2/R_Distro_Bus: track 121.7 -> 0.00 mm, vias 5 -> 0
- net /Mic Mux and Control/Dual Mic Distro Amp 3/R_Distro_Bus: track 120.5 -> 0.00 mm, vias 5 -> 0
- net /Mic Mux and Control/AMP-MIC-IN-5-6: track 97.9 -> 0.00 mm, vias 3 -> 0
- net /Mic Mux and Control/AMP-MIC-IN-4-6: track 95.6 -> 0.00 mm, vias 3 -> 0
- net /Mic Mux and Control/AMP-MIC-IN-5-4: track 93.1 -> 0.00 mm, vias 3 -> 0
- net /Mic Mux and Control/AMP-MIC-IN-4-4: track 89.4 -> 0.00 mm, vias 3 -> 0
- net /Mic Mux and Control/AMP-MIC-IN-5-7: track 89.4 -> 0.00 mm, vias 3 -> 0
- net /Mic Mux and Control/AMP-MIC-IN-5-2: track 87.2 -> 0.00 mm, vias 3 -> 0
- net /Mic Mux and Control/AMP-MIC-IN-5-5: track 84.7 -> 0.00 mm, vias 3 -> 0
- net /Mic Mux and Control/AMP-MIC-IN-4-2: track 84.1 -> 0.00 mm, vias 3 -> 0
- net /Mic Mux and Control/AMP-MIC-IN-4-7: track 83.0 -> 0.00 mm, vias 3 -> 0
- net /Mic Mux and Control/AMP-MIC-IN-4-5: track 80.1 -> 0.00 mm, vias 3 -> 0
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- added copper zone on F.Cu, net GNDREF
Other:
- board size 142.2 x 218.4 mm -> 142.2 x 214 mm
- net class 1A: clearance 0.127 -> 0.254; trace_width 0.381 -> 0.254
- net class 2A: clearance 0.127 -> 0.254
- net class 3A: clearance 0.127 -> 1.27
- net class GND: clearance 0.127 -> 0.254; trace_width 0.127 -> 0.254; via_dia 0.4572 -> 0.508

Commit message: About half way done with routing mic mux
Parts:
- moved C32 177.5 mm to (76.3, 247.0)
- moved C35 177.5 mm to (64.0, 247.7)
- moved C36 177.5 mm to (64.0, 249.8)
- moved R17 177.5 mm to (75.1, 260.8)
- moved C29 177.5 mm to (77.8, 258.6)
- moved C30 177.5 mm to (62.7, 258.6)
- moved C31 177.5 mm to (78.5, 247.0)
- moved C33 177.5 mm to (73.2, 243.2)
- moved C34 177.5 mm to (75.4, 243.2)
- moved R11 177.5 mm to (65.5, 256.2)
- moved R12 177.5 mm to (63.0, 256.7)
- moved R13 177.5 mm to (65.5, 260.8)
- moved R14 177.5 mm to (75.1, 256.4)
- moved R15 177.5 mm to (68.9, 253.1)
- moved R16 177.5 mm to (77.6, 256.6)
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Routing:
- net /2v5-SCL-0: track 0.00 -> 152.1 mm, vias 0 -> 3
- net /2v5-SDA-0: track 0.00 -> 142.5 mm, vias 0 -> 4
- net /Mic Mux and Control/Dual Mic Distro Amp 2/L_Distro_Bus: track 0.00 -> 135.2 mm, vias 0 -> 5
- net /Mic Mux and Control/AMP-MIC-IN-6-0: track 0.00 -> 132.9 mm, vias 0 -> 2
- net /Mic Mux and Control/AMP-MIC-IN-3-7: track 8.39 -> 140.4 mm, vias 1 -> 2
- net /Mic Mux and Control/AMP-MIC-IN-7-0: track 0.00 -> 129.3 mm, vias 0 -> 2
- net /Mic Mux and Control/AMP-MIC-IN-3-6: track 16.2 -> 144.8 mm, vias 1 -> 2
- net /Mic Mux and Control/AMP-MIC-IN-2-7: track 8.39 -> 134.0 mm, vias 1 -> 2
- net /Mic Mux and Control/Dual Mic Distro Amp 3/L_Distro_Bus: track 0.00 -> 125.3 mm, vias 0 -> 5
- net /Mic Mux and Control/AMP-MIC-IN-2-6: track 16.3 -> 141.3 mm, vias 1 -> 2
- net -12VA: track 50.0 -> 174.7 mm, vias 14 -> 24
- net /Mic Mux and Control/AMP-MIC-IN-6-7: track 0.00 -> 121.7 mm, vias 0 -> 2
- net /Mic Mux and Control/AMP-MIC-IN-6-1: track 0.00 -> 121.4 mm, vias 0 -> 2
- net /Mic Mux and Control/Dual Mic Distro Amp 2/R_Distro_Bus: track 0.00 -> 121.3 mm
- net /Mic Mux and Control/Dual Mic Distro Amp 3/R_Distro_Bus: track 0.00 -> 119.8 mm
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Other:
- net class 2A: trace_width 0.508 -> 0.254
